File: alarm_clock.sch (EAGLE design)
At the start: 33 parts, among them IC1 DS1307, J1 USB-MICROB", Q1 16MHz, U1 ATMEGA328P-PU, U2 MC14489BPE

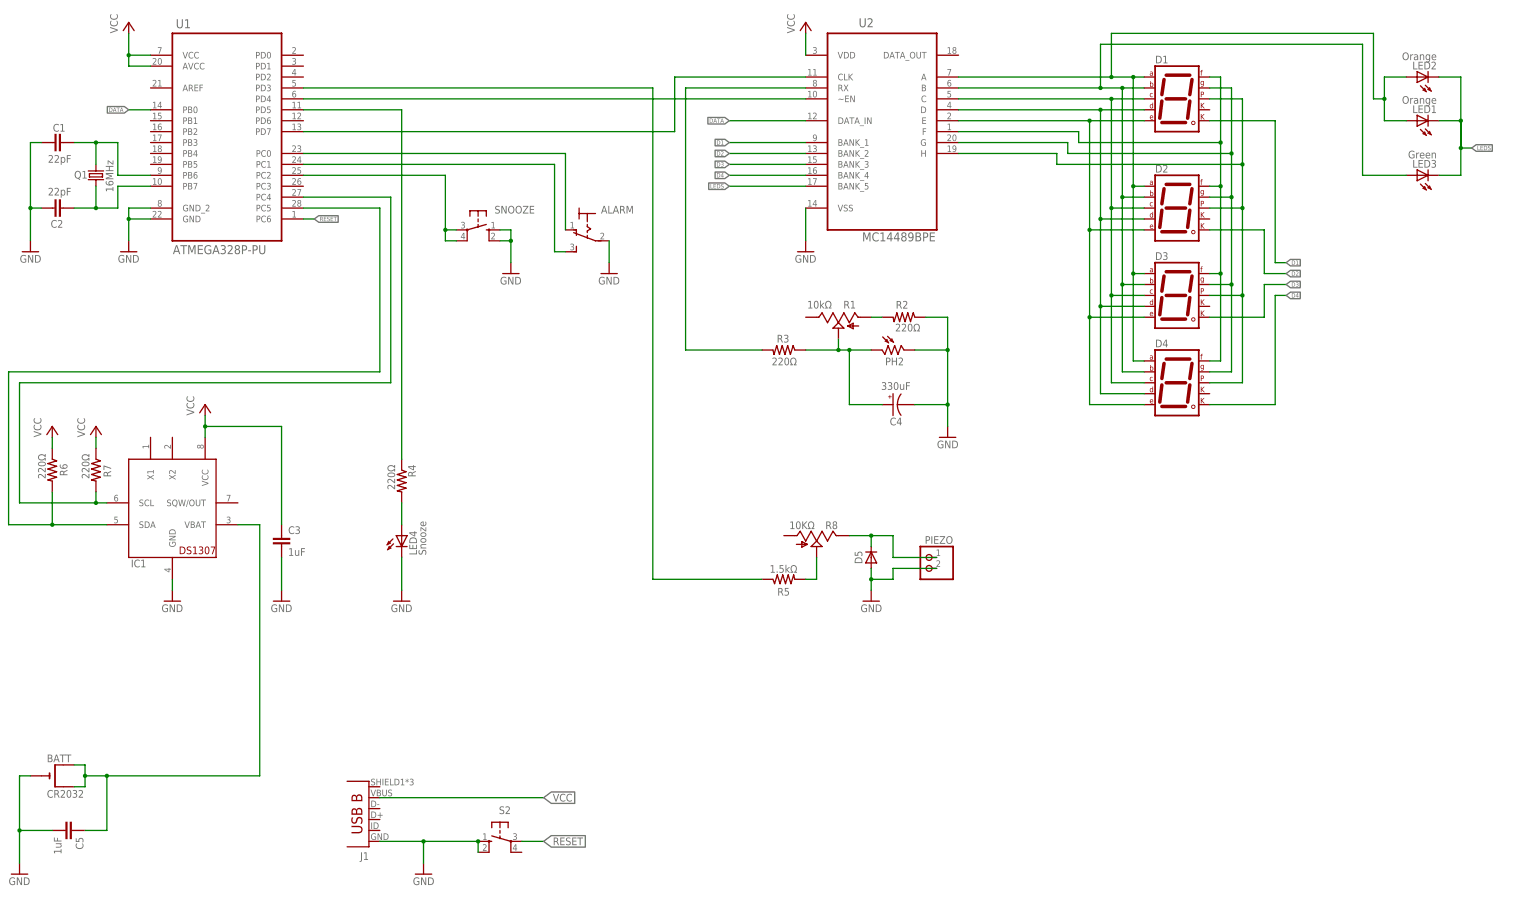
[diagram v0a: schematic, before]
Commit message: Snooze LED and push-button omitted in lue of external, wired button with integral LED. Minor amends:
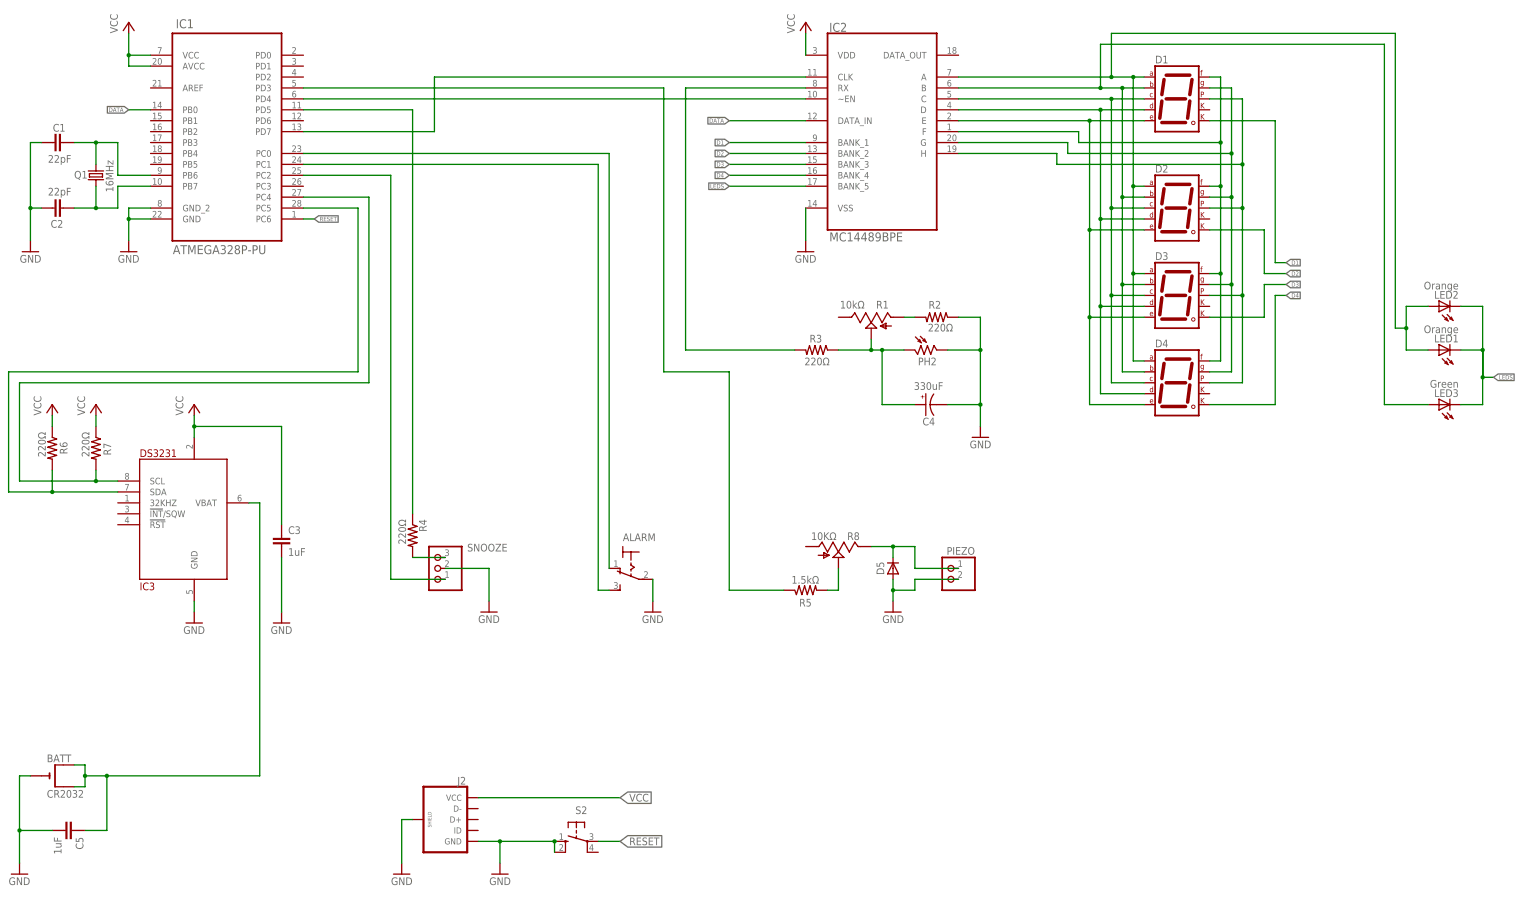
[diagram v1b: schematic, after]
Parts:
- removed J1: USB-MICROB", SparkFun-Connectors:USB-MICROB"
- removed LED4: Snooze, led:LED10MM
- removed U1: ATMEGA328P-PU, Atmel_By_element14_Batch_1-00:ATMEGA328P-PU
- added IC3: DS3231, ds3231:DS3231
- added J2: (no value), SparkFun-Connectors:USB_MICROB_PLUG-PTH2
- IC1: value DS1307 -> ATMEGA328P-PU; device adafruit:DS1307 -> Atmel_By_element14_Batch_1-00:ATMEGA328P-PU; MF MAXIM INTEGRATED PRODUCTS -> ATMEL; MPN DS3231MZ+TRL -> (none); OC_FARNELL 2515487 -> (none)
- LED1, LED2, LED3: device led:LED5MM -> led:LED3MM
- PIEZO: device pinhead:PINHD-1X2 -> pinhead:PINHD-1X2/90
- SNOOZE: device switch-omron:10-XX -> pinhead:PINHD-1X3/90
- renumbered U2 to IC2
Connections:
- net CLK: now also IC1.PD7; no longer U1.PD7
- net DATA: now also IC1.PB0; no longer U1.PB0
- net EN: now also IC1.PD4; no longer U1.PD4
- net GND: now also IC1.GND_2, IC3.GND, J2.GND, J2.SHIELD, SNOOZE.2; no longer J1.GND, LED4.C, SNOOZE.S, SNOOZE.S1, U1.GND, U1.GND_2
- net N$18: now also IC1.PB7; no longer U1.PB7
- net N$19: now also IC1.PB6; no longer U1.PB6
- net N$2: now also SNOOZE.3; no longer LED4.A
- net N$5: now also IC1.PC0; no longer U1.PC0
- net N$6: now also IC1.PC1; no longer U1.PC1
- net N$9: now also IC1.PC2, SNOOZE.1; no longer SNOOZE.P, SNOOZE.P1, U1.PC2
- net PZ: now also IC1.PD3; no longer U1.PD3
- net RESET: now also IC1.PC6; no longer U1.PC6
- net SCL: now also IC1.PC4, IC3.SCL; no longer IC1.SCL, U1.PC4
- net SDA: now also IC1.PC5, IC3.SDA; no longer IC1.SDA, U1.PC5
- net SNZ: now also IC1.PD5; no longer U1.PD5
- net VBAT: now also IC3.VBAT; no longer IC1.VBAT
- net VCC: now also IC1.AVCC, IC3.VCC, J2.VCC; no longer J1.VBUS, U1.AVCC, U1.VCC
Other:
- note added: "Input: Alarm Toggle"
- note added: "Intput/Output: Snooze - Large Red LED - Button"
- note removed: "Output: Snooze - Large Red LED"
- moved on the sheet: ALARM, C4, D5, LED1, LED2, LED3, PH2, PIEZO, R1, R2, R3, R4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

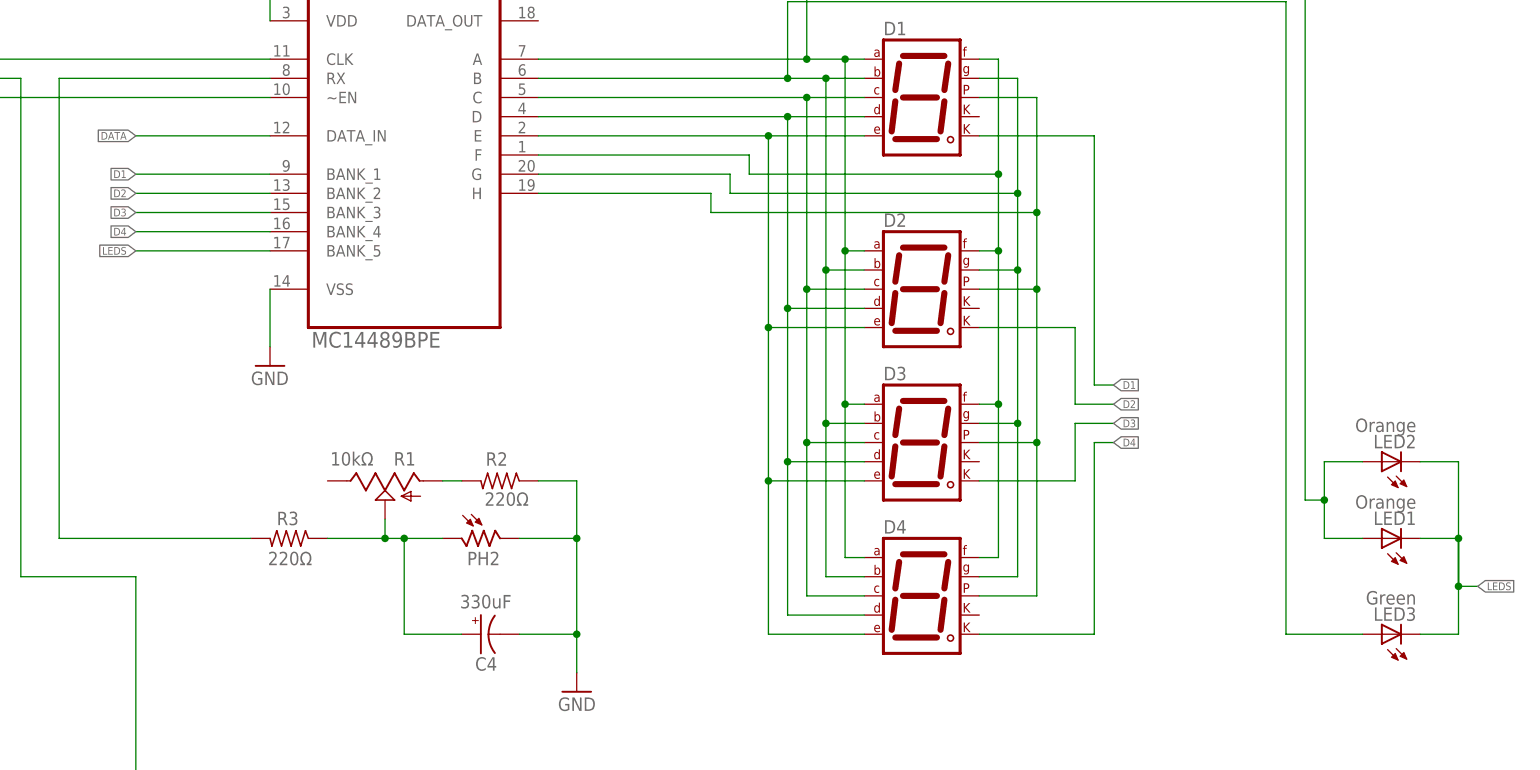
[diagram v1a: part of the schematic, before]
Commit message: Initial board set-up (no routes):
Initial board set-up (pre route) with toggle switch on pcb and pin connectors
shown on reverse side of board.
Schematic amended accordingly.
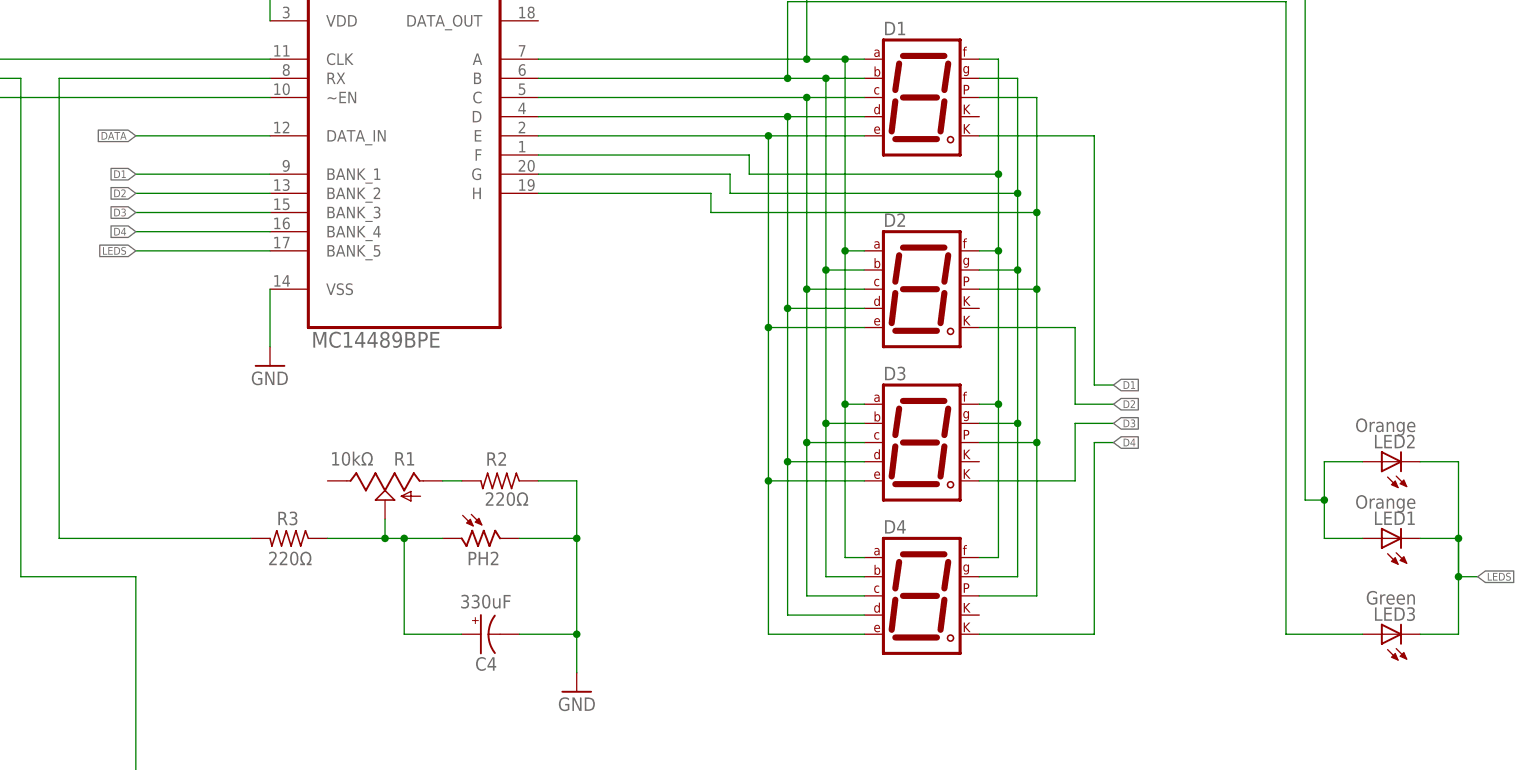
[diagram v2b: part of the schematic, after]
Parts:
- ALARM: value (none) -> S1
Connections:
- removed net N$3: IC2.DATA_IN
- net DATA: now also IC2.DATA_IN

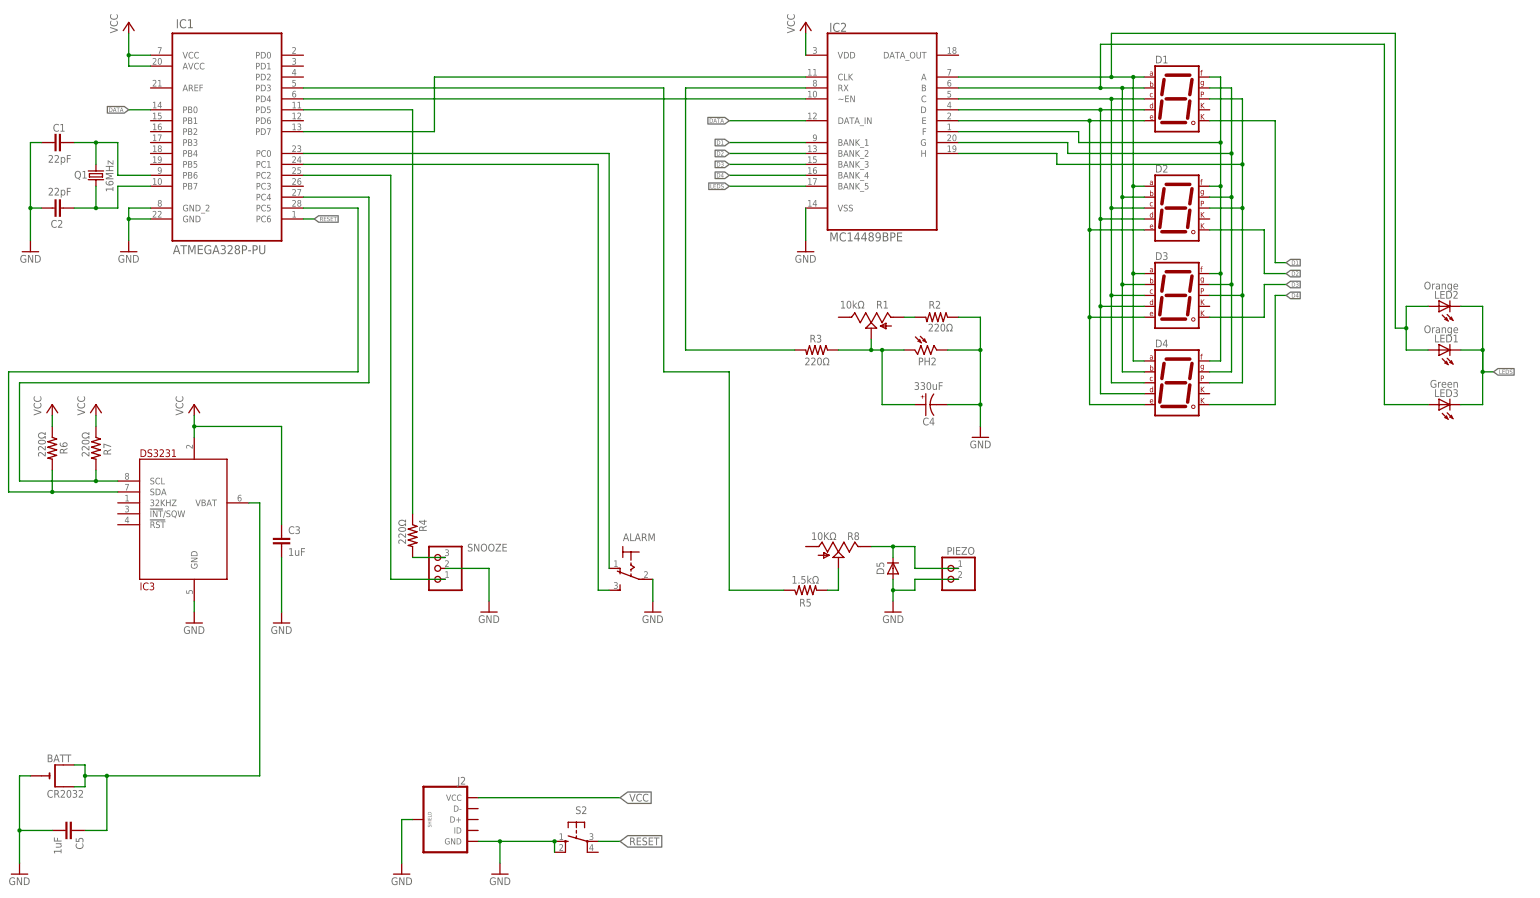
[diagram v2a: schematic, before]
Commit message: Replaced toggle switch & green led with connectors:
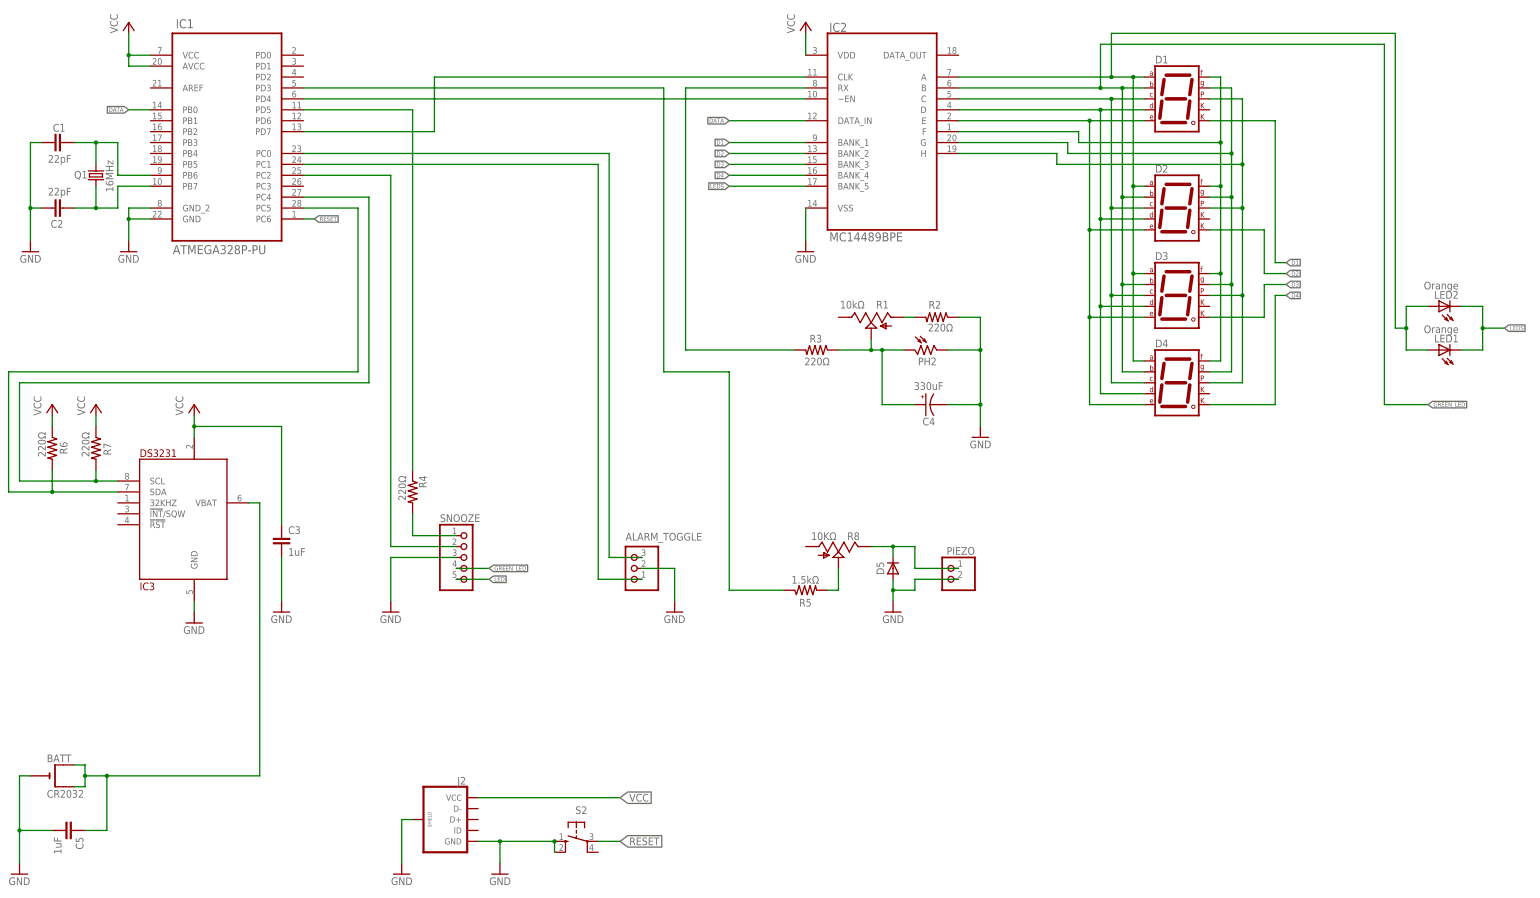
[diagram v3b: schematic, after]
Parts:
- removed ALARM: S1, switch:320-916
- removed LED3: Green, led:LED3MM
- added ALARM_TOGGLE: (no value), pinhead:PINHD-1X3/90
- SNOOZE: device pinhead:PINHD-1X3/90 -> pinhead:PINHD-1X5/90
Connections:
- removed net B: D1.B, D2.B, D3.B, D4.B, IC2.B, LED3.A
- new net GREEN_LED: D1.B, D2.B, D3.B, D4.B, IC2.B, SNOOZE.4
- new net LED: SNOOZE.5
- net GND: now also ALARM_TOGGLE.2, SNOOZE.3; no longer ALARM.P, SNOOZE.2
- net LEDS: no longer LED3.C
- net N$2: now also SNOOZE.1; no longer SNOOZE.3
- net N$5: now also ALARM_TOGGLE.3; no longer ALARM.O
- net N$6: now also ALARM_TOGGLE.1; no longer ALARM.S
- net N$9: now also SNOOZE.2; no longer SNOOZE.1
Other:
- moved on the sheet: R4
